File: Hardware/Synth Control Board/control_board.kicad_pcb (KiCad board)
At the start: 2 copper layers, 56 parts, among them J1 Conn_01x13, J10 Conn_01x05, J11 Conn_01x08, J12 Conn_01x06, J2 Conn_01x03, J3 Conn_01x13, J4 Conn_01x13, J5 Conn_01x02, J6 Conn_01x13, J7 Conn_01x05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

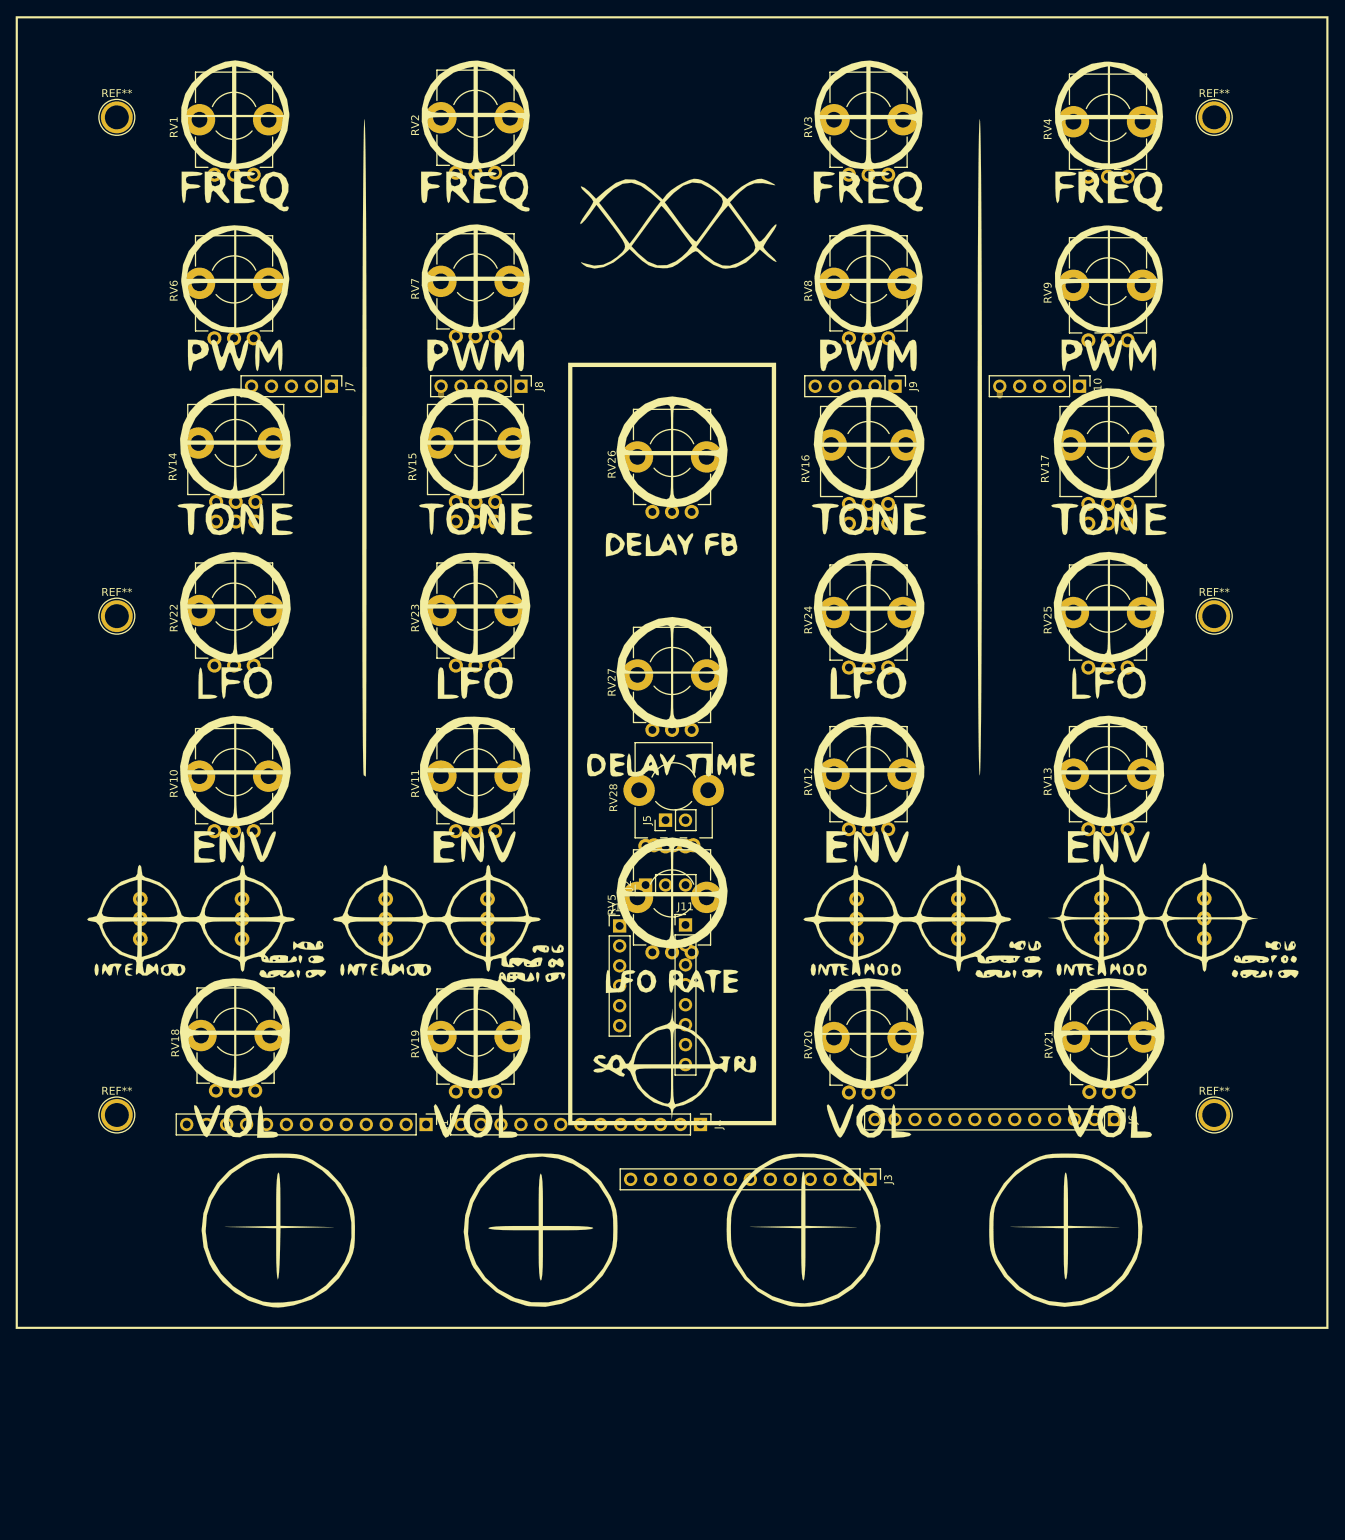
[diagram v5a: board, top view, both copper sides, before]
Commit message: tentative edge cut on control board update
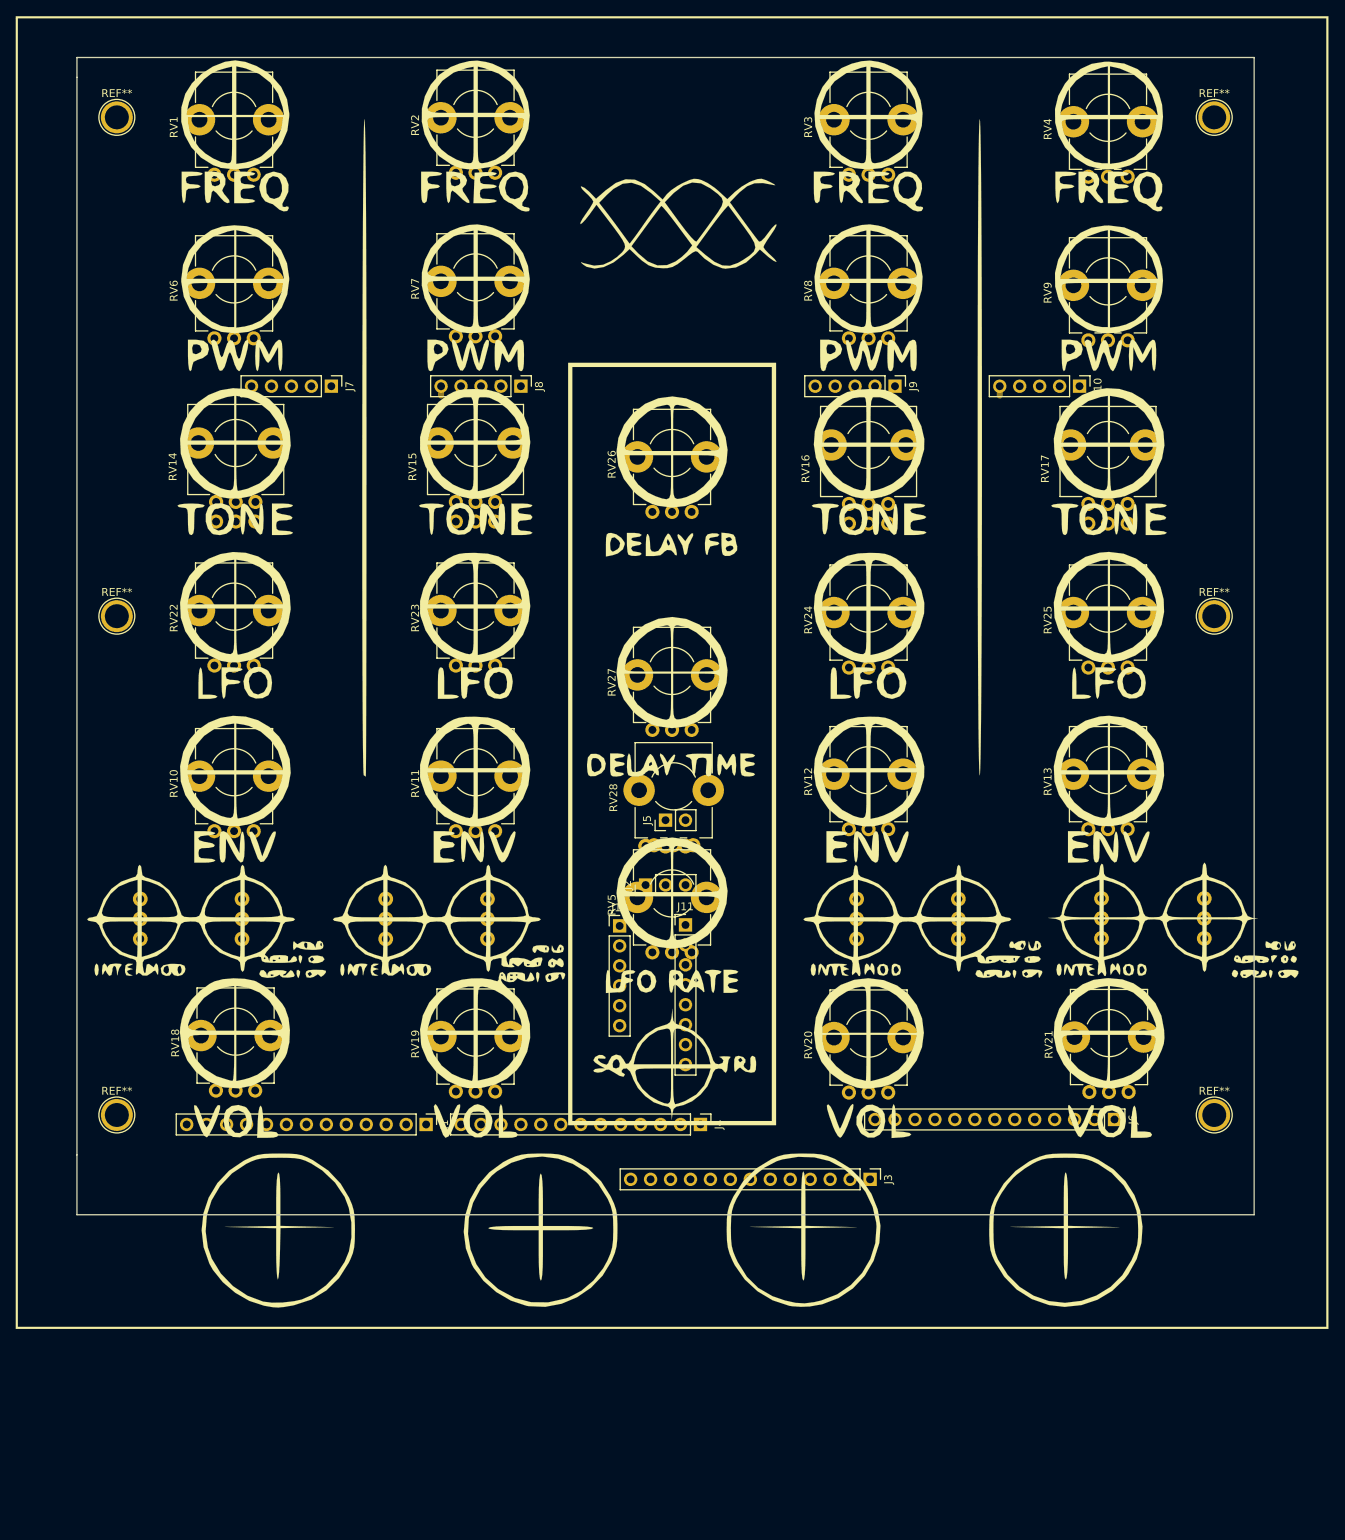
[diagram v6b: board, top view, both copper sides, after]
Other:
- board outline added: 149.9 x 147.3 mm
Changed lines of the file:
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@@
     (area -0.375448 -0.375448 167.139817 167.139817)
     (thickness 1.6)
-    (drawings 0)
+    (drawings 6)
     (tracks 5)
     (zones 0)
@@
       (xy 0.164846 -35.019475) (xy 1.93367 -34.772762)) (layer F.SilkS) (width 0.01))
   )
+  (gr_line (start 7.62 5.08) (end 7.62 7.62) (layer Edge.Cuts) (width 0.15))
+  (gr_line (start 157.48 5.08) (end 7.62 5.08) (layer Edge.Cuts) (width 0.15))
+  (gr_line (start 157.48 152.4) (end 157.48 5.08) (layer Edge.Cuts) (width 0.15))
+  (gr_line (start 7.62 152.4) (end 157.48 152.4) (layer Edge.Cuts) (width 0.15))
+  (gr_line (start 7.62 144.78) (end 7.62 152.4) (layer Edge.Cuts) (width 0.15))
+  (gr_line (start 7.62 7.62) (end 7.62 144.78) (layer Edge.Cuts) (width 0.15))
   (segment (start 37.298 46.7595) (end 37.465 46.9265) (width 0.762) (layer F.Cu) (net 6))
   (segment (start 61.174 46.5055) (end 61.595 46.9265) (width 0.762) (layer F.Cu) (net 20))

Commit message: fix delay controls on panel artwork and control board layout
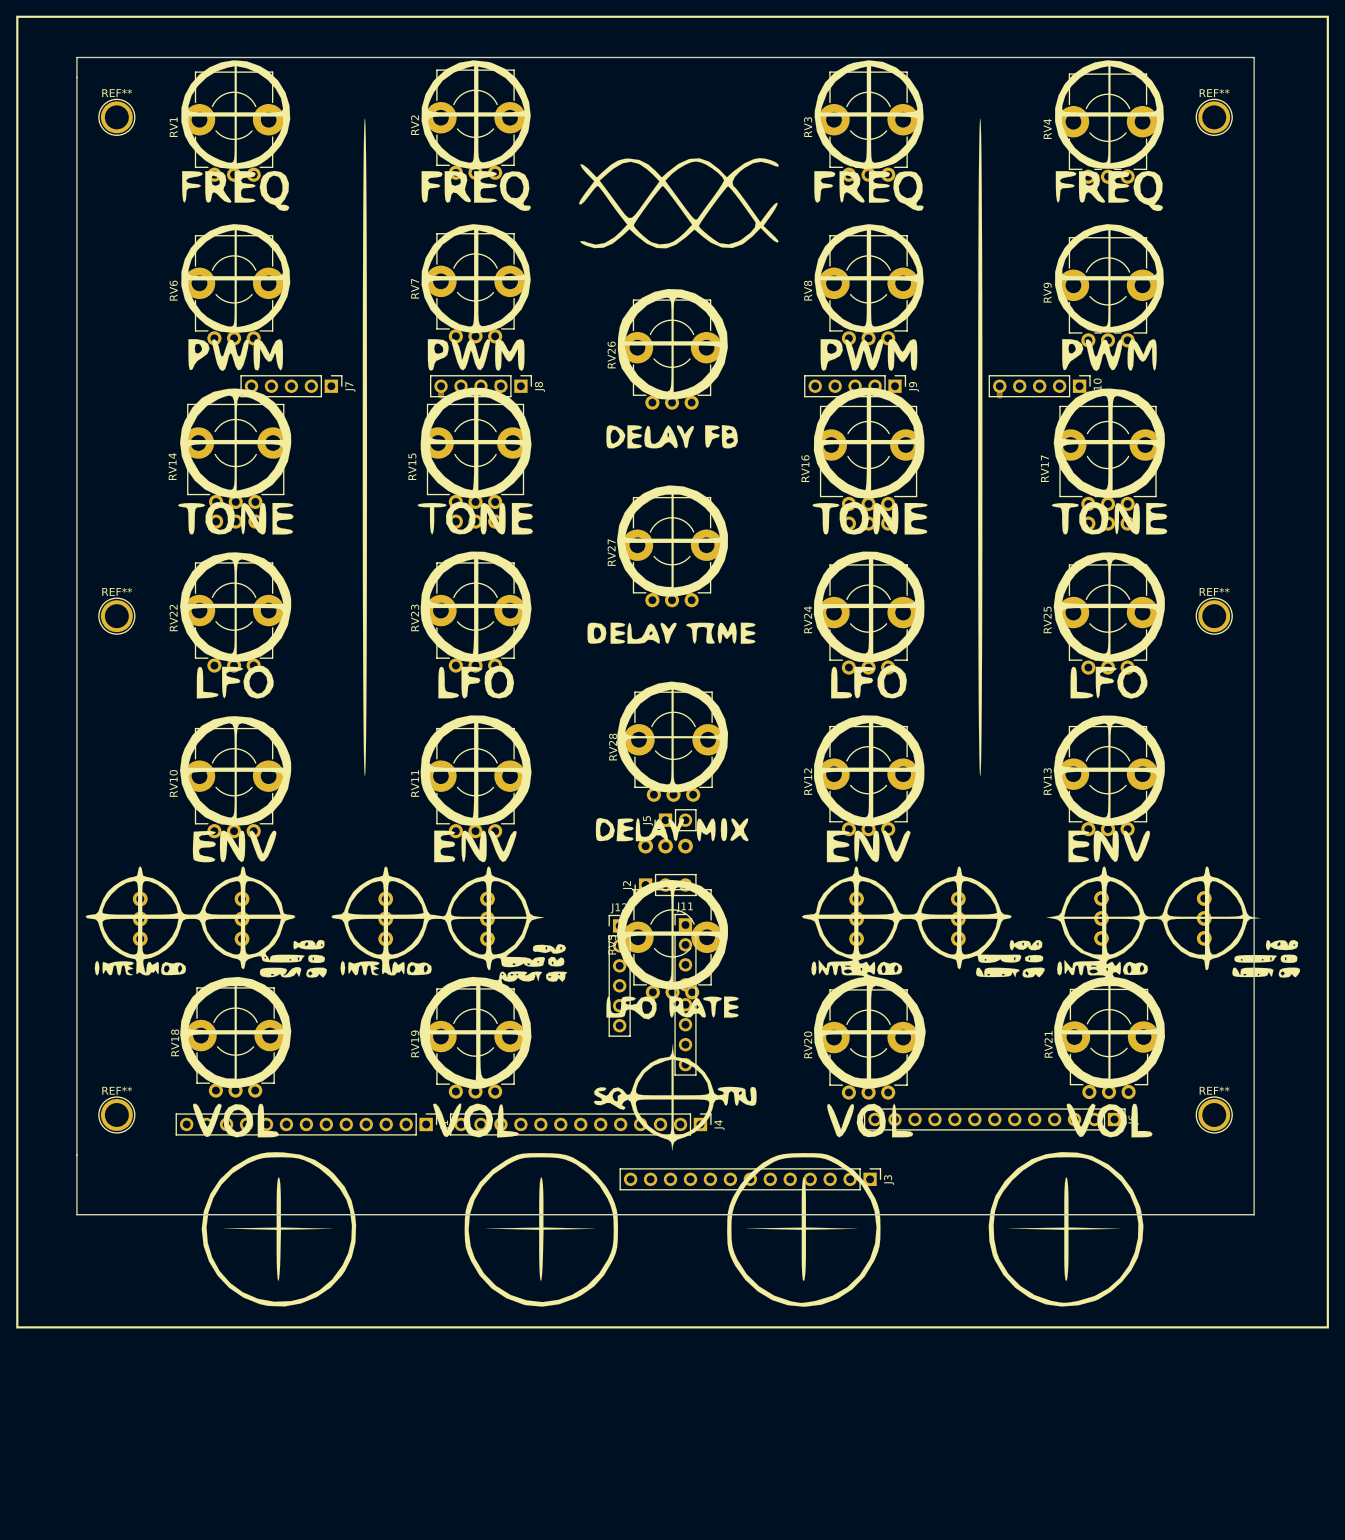
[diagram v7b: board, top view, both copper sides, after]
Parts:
- moved RV27 16.5 mm to (85.9, 74.2)
- moved RV26 13.9 mm to (85.9, 49.0)
- moved RV28 6.43 mm to (86.1, 98.9)
- moved RV5 5.08 mm to (85.9, 124.1)
- moved G*** 0.09 mm to (83.3, 83.2)

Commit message: move main synth board so that connector dimensions match between boards.
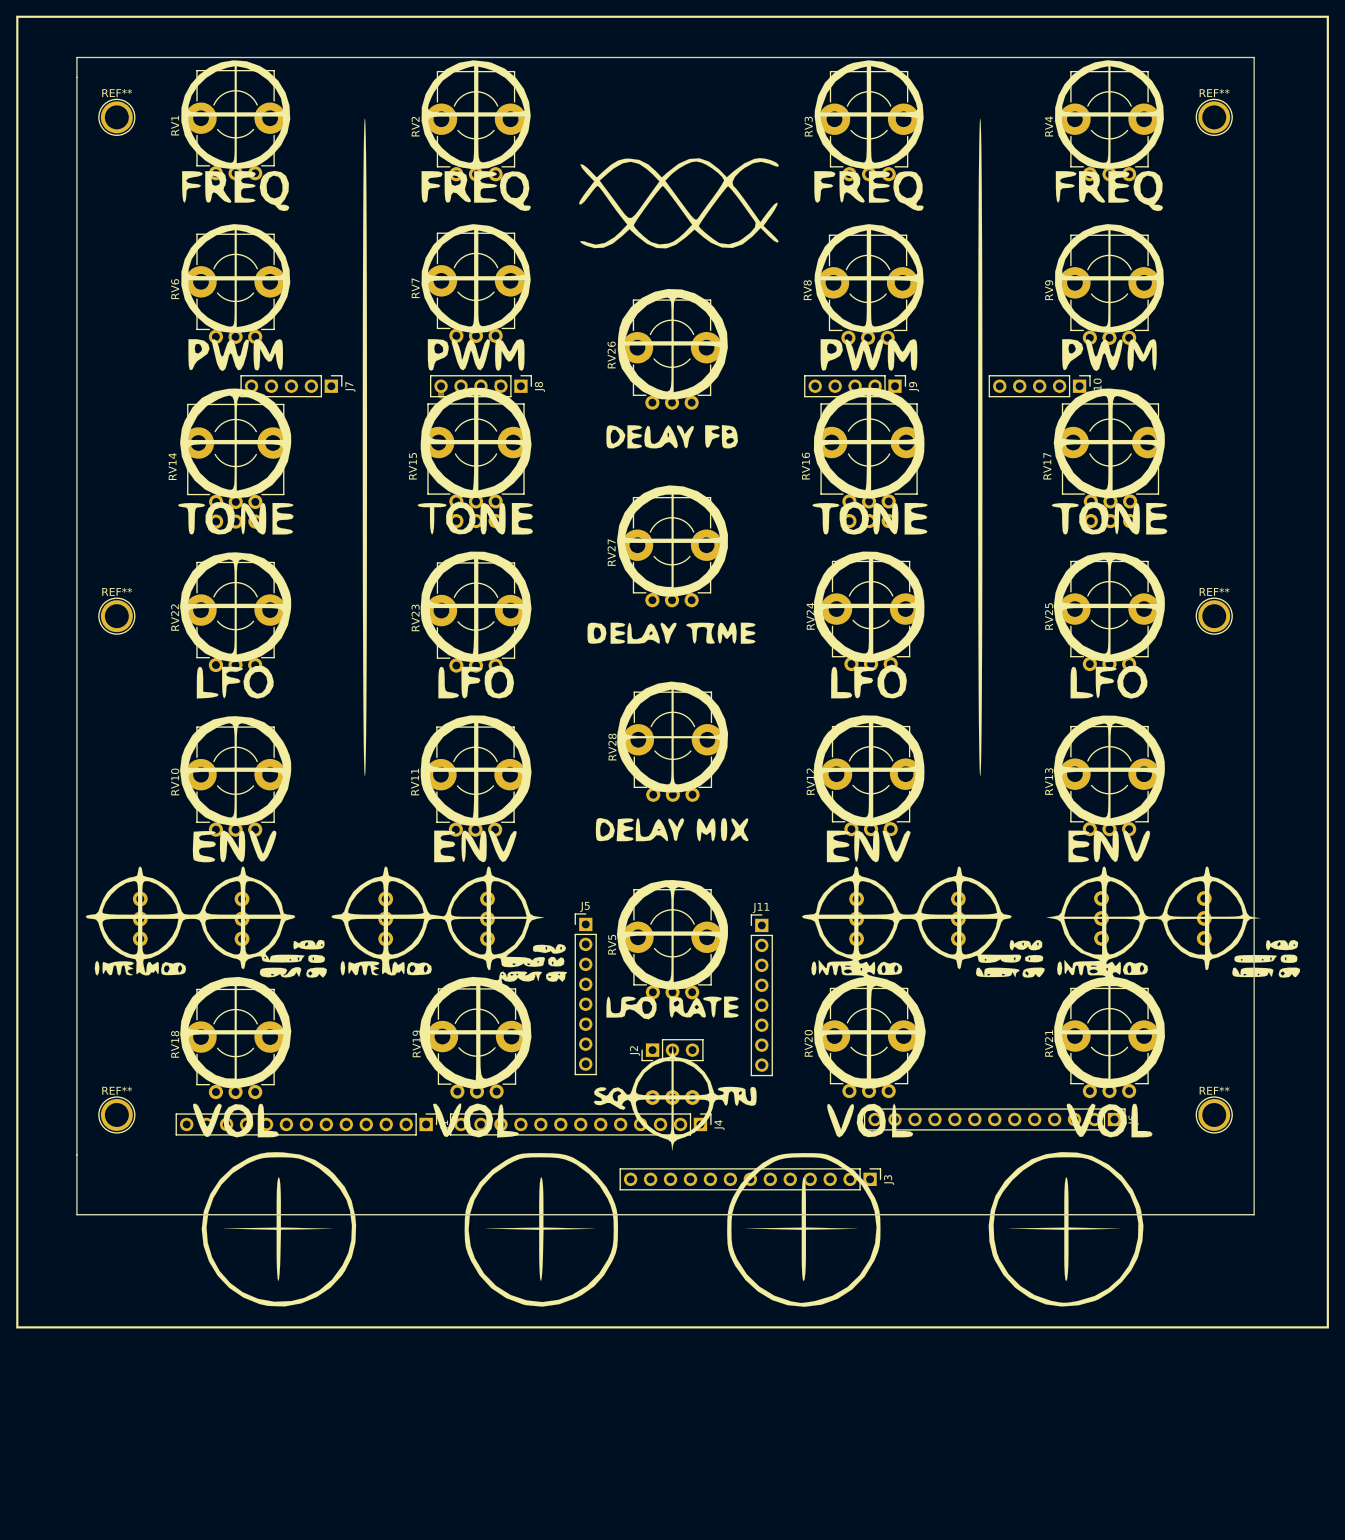
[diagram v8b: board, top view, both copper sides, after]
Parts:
- removed J12: Conn_01x06, Pin_Headers:Pin_Header_Straight_1x06_Pitch2.54mm
- J5: value Conn_01x02 -> Conn_01x08; footprint Pin_Headers:Pin_Header_Straight_1x02_Pitch2.54mm -> Pin_Headers:Pin_Header_Straight_1x08_Pitch2.54mm
- RV26: value 100kA -> 50kA
- RV27: value 100kA -> 20kA
- RV28: value 100kA -> 50k
- moved SW1 32.0 mm to (83.4, 137.5)
- moved J2 21.0 mm to (80.9, 131.4)
- moved J5 16.7 mm to (72.4, 115.4), turned to 0 degrees
- moved J11 9.72 mm to (94.8, 115.6)
- moved RV24 0.55 mm to (111.2, 82.3)
- moved RV25 0.48 mm to (141.6, 82.3)
- moved RV17 0.45 mm to (141.7, 61.6)
- moved RV4 0.37 mm to (141.6, 19.9)
- moved RV9 0.37 mm to (141.6, 40.8)
- moved RV16 0.32 mm to (111.0, 61.6)
- moved RV12 0.32 mm to (111.2, 103.3)
- moved RV1 0.27 mm to (30.3, 19.8)
- moved RV10 0.27 mm to (30.3, 103.4)
- moved RV6 0.27 mm to (30.3, 40.6)
- moved RV20 0.20 mm to (111.0, 136.7)
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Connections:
- J5 pad 1: /LFO_freq_in -> /delay_in_1
- J5 pad 2: /LFO_freq_out -> /delay_out_1
- RV28 pad 2: /delay_out_3 -> GND
- RV28 pad 3: GND -> /delay_out_3
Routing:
- net /lfo_out_4: track 1.20 -> 0.00 mm
